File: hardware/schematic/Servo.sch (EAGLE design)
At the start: 23 parts

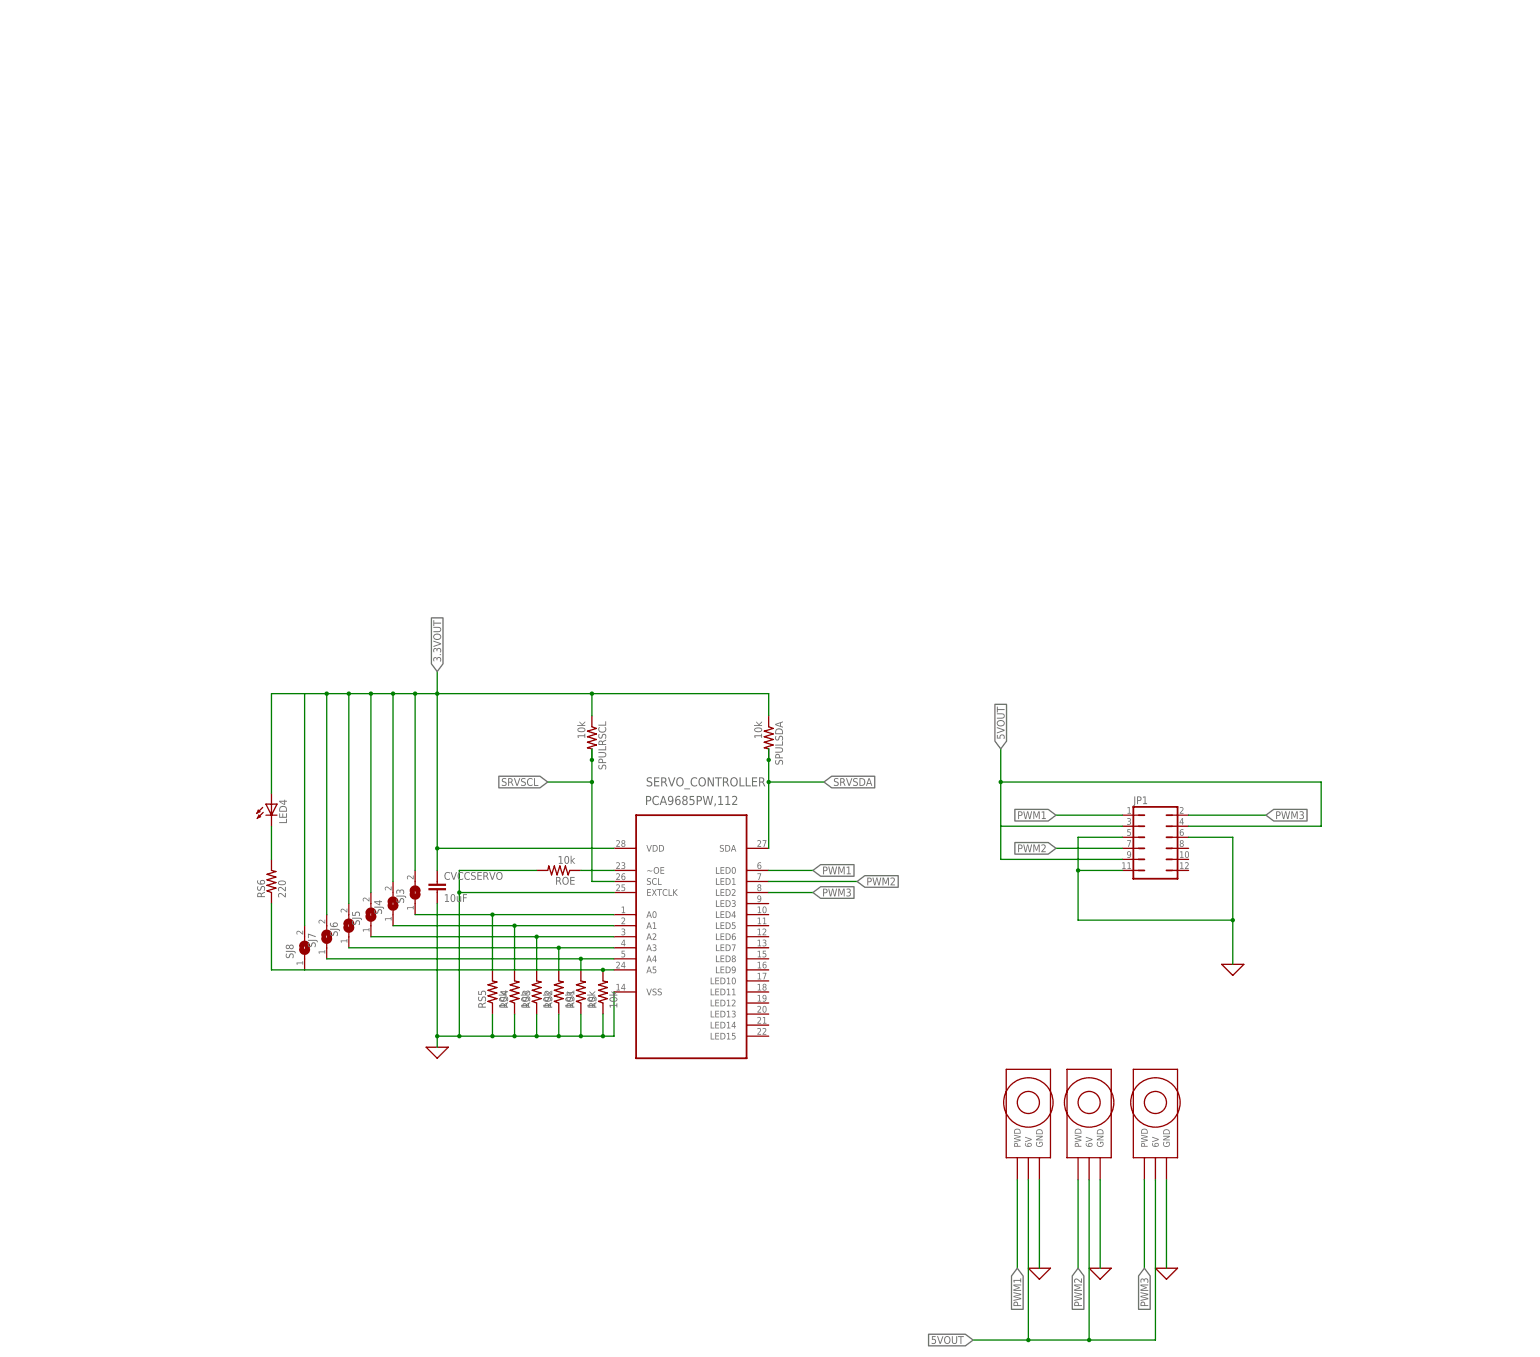
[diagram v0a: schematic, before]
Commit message: Schematic Updates
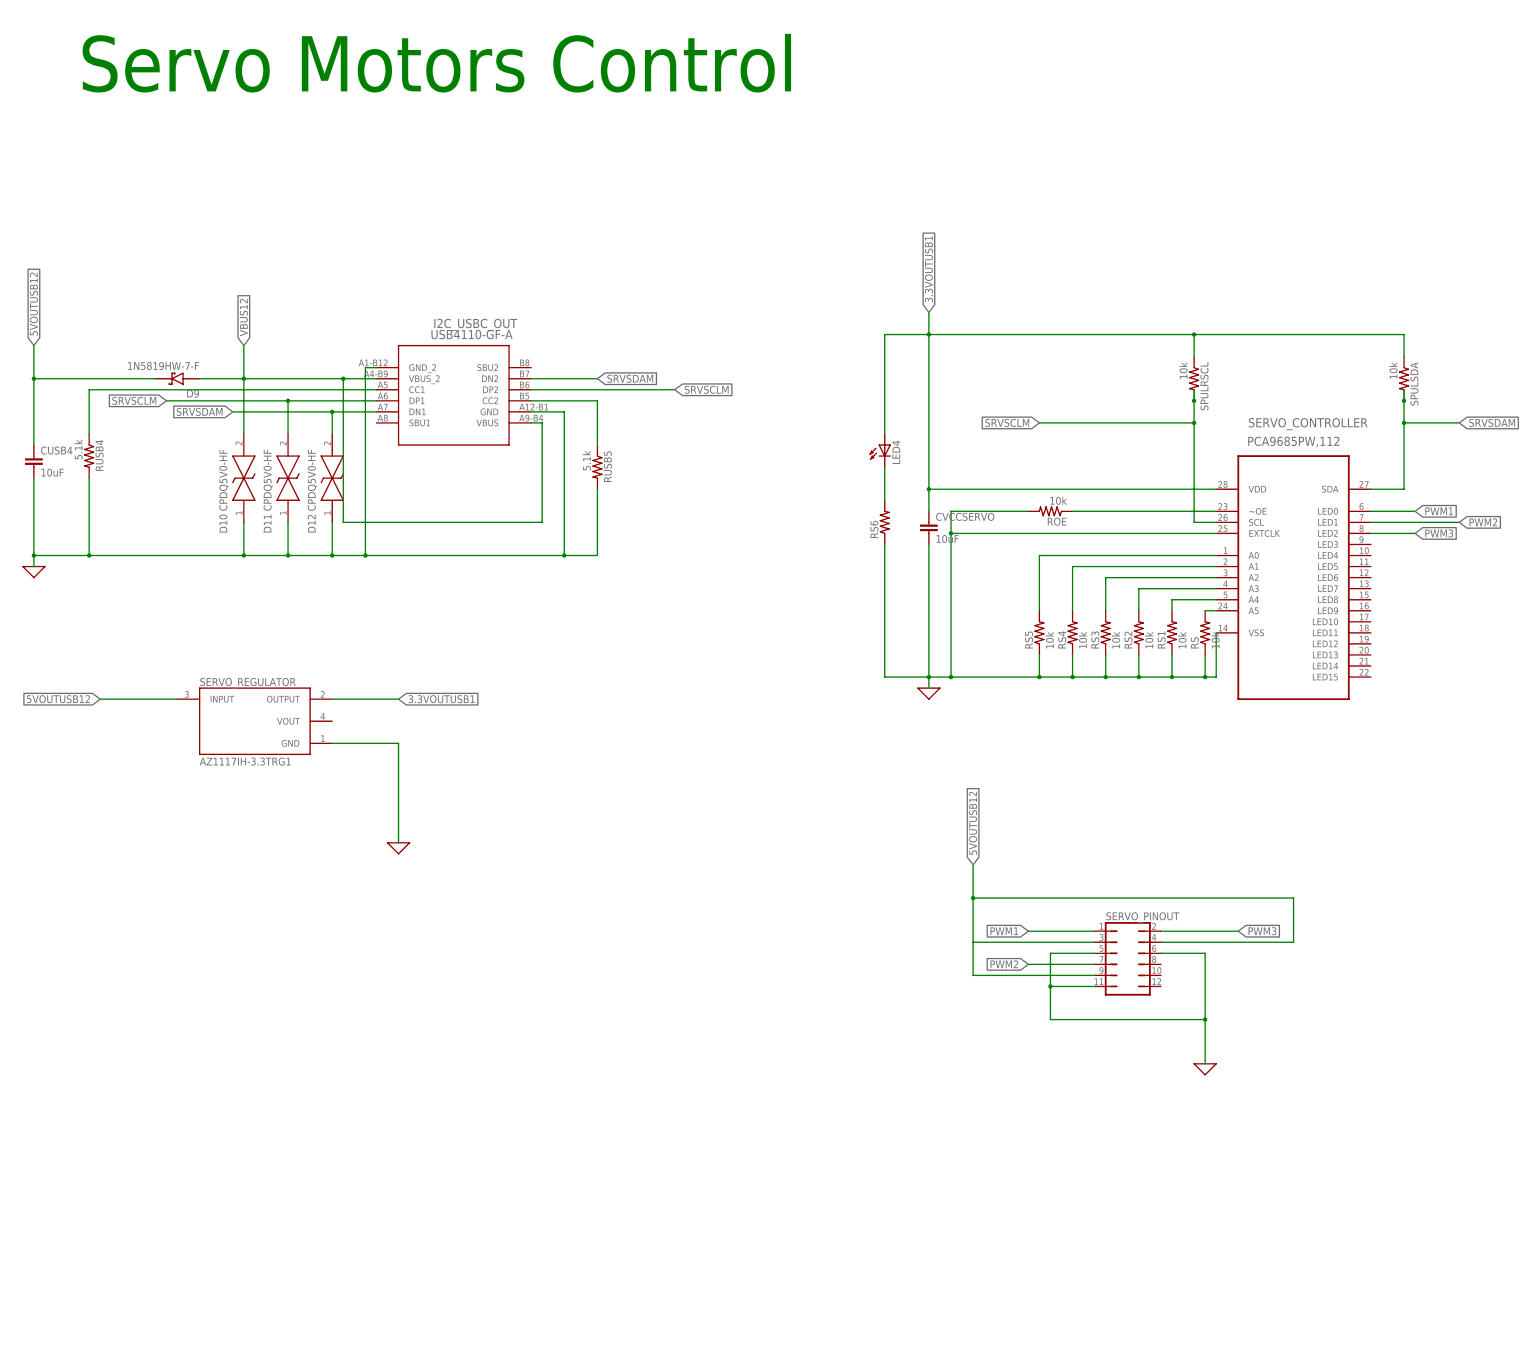
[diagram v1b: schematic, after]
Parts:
- removed JP1: (no value), jumper:JP6Q
- removed SJ3, SJ4, SJ5, SJ6, SJ7, SJ8: (no value), jumper:SJ
- removed U$1, U$2, U$3: SERVO, Motors:SERVO
- added CUSB4: 10uF, rcl:C-EUC0805
- added D10, D11, D12: CPDQ5V0-HF, CPDQ5V0-HF:CPDQ5V0-HF
- added D9: 1N5819HW-7-F, 1N5819HW-7-F:1N5819HW-7-F
- added I2C_USBC_OUT: USB4110-GF-A, USB4110-GF-A:USB4110-GF-A
- added RUSB4, RUSB5: 5.1k, rcl:R-US_M0805
- added SERVO_PINOUT: (no value), jumper:JP6Q
- added SERVO_REGULATOR: AZ1117IH-3.3TRG1, AZ1117IH-3.3TRG1:AZ1117IH-3.3TRG1
- RS6: value 220 -> 2.2k
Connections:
- removed net 0: CVCCSERVO.2, JP1.11, JP1.5, JP1.6, ROE.2, RS.1, RS1.1, RS2.1, RS3.1, RS4.1, RS5.1, SERVO_CONTROLLER.EXTCLK, SERVO_CONTROLLER.VSS, U$1.GND, U$2.GND, U$3.GND
- removed net 3.3VOUT: CVCCSERVO.1, LED4.A, SERVO_CONTROLLER.VDD, SJ3.2, SJ4.2, SJ5.2, SJ6.2, SJ7.2, SJ8.2, SPULRSCL.1, SPULSDA.1
- removed net 5VOUT: JP1.3, JP1.4, JP1.9, U$1.6V, U$2.6V, U$3.6V
- removed net SRVSCL: SERVO_CONTROLLER.SCL, SPULRSCL.2
- removed net SRVSDA: SERVO_CONTROLLER.SDA, SPULSDA.2
- new net 3.3VOUTUSB1: CVCCSERVO.1, LED4.A, SERVO_CONTROLLER.VDD, SERVO_REGULATOR.OUTPUT, SPULRSCL.1, SPULSDA.1
- new net 5VOUTUSB12: CUSB4.1, D9.K, SERVO_PINOUT.3, SERVO_PINOUT.4, SERVO_PINOUT.9, SERVO_REGULATOR.INPUT
- new net GND: CUSB4.2, CVCCSERVO.2, D10.K, D11.K, D12.K, I2C_USBC_OUT.GND, I2C_USBC_OUT.GND_2, ROE.2, RS.1, RS1.1, RS2.1, RS3.1, RS4.1, RS5.1, RS6.1, RUSB4.2, RUSB5.2, SERVO_CONTROLLER.EXTCLK, SERVO_CONTROLLER.VSS, SERVO_PINOUT.11, SERVO_PINOUT.5, SERVO_PINOUT.6, SERVO_REGULATOR.GND
- new net N$64: I2C_USBC_OUT.CC1, RUSB4.1
- new net N$65: I2C_USBC_OUT.CC2, RUSB5.1
- new net SRVSCLM: D11.A, I2C_USBC_OUT.DP1, I2C_USBC_OUT.DP2, SERVO_CONTROLLER.SCL, SPULRSCL.2
- new net SRVSDAM: D12.A, I2C_USBC_OUT.DN1, I2C_USBC_OUT.DN2, SERVO_CONTROLLER.SDA, SPULSDA.2
- new net VBUS12: D10.A, D9.A, I2C_USBC_OUT.VBUS, I2C_USBC_OUT.VBUS_2
- net N$44: no longer SJ4.1
- net N$45: no longer SJ3.1
- net N$46: no longer SJ5.1
- net N$47: no longer SJ6.1
- net N$48: no longer SJ7.1
- net N$49: no longer RS6.1, SJ8.1
- net PWM1: now also SERVO_PINOUT.1; no longer JP1.1, U$1.PWD
- net PWM2: now also SERVO_PINOUT.7; no longer JP1.7, U$2.PWD
- net PWM3: now also SERVO_PINOUT.2; no longer JP1.2, U$3.PWD
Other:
- note added: "Servo Motors Control"
- moved on the sheet: CVCCSERVO, LED4, ROE, RS, RS1, RS2, RS3, RS4, RS5, RS6, SERVO_CONTROLLER, SPULRSCL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

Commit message: Update Servo.sch
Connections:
- net N$39 renamed OE
- net N$44 renamed A1
- net N$45 renamed A0
- net N$46 renamed A2
- net N$47 renamed A3
- net N$48 renamed A4
- net N$49 renamed A5
- net N$50 renamed LED_RS6
- net N$64 renamed CC1_RUSB4
- net N$65 renamed CC2
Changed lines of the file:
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@@
 </segment>
 </net>
-<net name="N$39" class="0">
+<net name="OE" class="0">
 <segment>
 <pinref part="SERVO_CONTROLLER" gate="A" pin="~OE"/>
@@
 </segment>
 </net>
-<net name="N$45" class="0">
+<net name="A0" class="0">
 <segment>
 <pinref part="SERVO_CONTROLLER" gate="A" pin="A0"/>
@@
 </segment>
 </net>
-<net name="N$44" class="0">
+<net name="A1" class="0">
 <segment>
 <pinref part="SERVO_CONTROLLER" gate="A" pin="A1"/>
@@
 </segment>
 </net>
-<net name="N$46" class="0">
+<net name="A2" class="0">
 <segment>
 <pinref part="SERVO_CONTROLLER" gate="A" pin="A2"/>
@@
 </segment>
 </net>
-<net name="N$47" class="0">
+<net name="A3" class="0">
 <segment>
 <pinref part="SERVO_CONTROLLER" gate="A" pin="A3"/>
@@
 </segment>
 </net>
-<net name="N$48" class="0">
+<net name="A4" class="0">
 <segment>
 <pinref part="SERVO_CONTROLLER" gate="A" pin="A4"/>
@@
 </segment>
 </net>
-<net name="N$49" class="0">
+<net name="A5" class="0">
 <segment>
 <pinref part="SERVO_CONTROLLER" gate="A" pin="A5"/>
@@
 </segment>
 </net>
-<net name="N$50" class="0">
+<net name="LED_RS6" class="0">
 <segment>
 <pinref part="LED4" gate="G$1" pin="C"/>
@@
 <pinref part="SPULRSCL" gate="G$1" pin="2"/>
 <wire x1="83.82" y1="111.76" x2="83.82" y2="116.84" width="0.1524" layer="91"/>
-<wire x1="83.82" y1="116.84" x2="83.82" y2="119.38" width="0.1524" layer="91"/>
-<junction x="83.82" y="116.84"/>
 <wire x1="83.82" y1="111.76" x2="48.26" y2="111.76" width="0.1524" layer="91"/>
 <junction x="83.82" y="111.76"/>
@@
 </segment>
 </net>
-<net name="N$64" class="0">
+<net name="CC1_RUSB4" class="0">
 <segment>
 <pinref part="I2C_USBC_OUT" gate="A" pin="CC1"/>
@@
 </segment>
 </net>
-<net name="N$65" class="0">
+<net name="CC2" class="0">
 <segment>
 <pinref part="I2C_USBC_OUT" gate="A" pin="CC2"/>

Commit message: Schematics updates
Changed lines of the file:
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@@
 <parts>
 <part name="SERVO_CONTROLLER" library="PCA9685PW_112" deviceset="PCA9685PW,112" device=""/>
-<part name="X_8" library="ngspice-simulation" library_urn="urn:adsk.eagle:library:527439" deviceset="GND" device=""/>
 <part name="CVCCSERVO" library="rcl" library_urn="urn:adsk.eagle:library:334" deviceset="C-EU" device="C0805" package3d_urn="urn:adsk.eagle:package:23617/2" value="10uF"/>
-<part name="X_9" library="ngspice-simulation" library_urn="urn:adsk.eagle:library:527439" deviceset="GND" device=""/>
 <part name="ROE" library="rcl" library_urn="urn:adsk.eagle:library:334" deviceset="R-US_" device="M0805" package3d_urn="urn:adsk.eagle:package:23556/2" value="10k"/>
 <part name="SPULRSCL" library="rcl" library_urn="urn:adsk.eagle:library:334" deviceset="R-US_" device="M0805" package3d_urn="urn:adsk.eagle:package:23556/2" value="10k"/>
@@
 <part name="D9" library="1N5819HW-7-F" deviceset="1N5819HW-7-F" device=""/>
 <part name="CUSB4" library="rcl" library_urn="urn:adsk.eagle:library:334" deviceset="C-EU" device="C0805" package3d_urn="urn:adsk.eagle:package:23617/2" value="10uF"/>
-<part name="X_16" library="ngspice-simulation" library_urn="urn:adsk.eagle:library:527439" deviceset="GND" device=""/>
 <part name="RUSB4" library="rcl" library_urn="urn:adsk.eagle:library:334" deviceset="R-US_" device="M0805" package3d_urn="urn:adsk.eagle:package:23556/2" value="5.1k"/>
 <part name="RUSB5" library="rcl" library_urn="urn:adsk.eagle:library:334" deviceset="R-US_" device="M0805" package3d_urn="urn:adsk.eagle:package:23556/2" value="5.1k"/>
@@
 <part name="D12" library="CPDQ5V0-HF" deviceset="CPDQ5V0-HF" device=""/>
 <part name="SERVO_REGULATOR" library="AZ1117IH-3.3TRG1" deviceset="AZ1117IH-3.3TRG1" device=""/>
-<part name="X_21" library="ngspice-simulation" library_urn="urn:adsk.eagle:library:527439" deviceset="GND" device=""/>
+<part name="SUPPLY1" library="supply2" library_urn="urn:adsk.eagle:library:372" deviceset="GND" device=""/>
+<part name="SUPPLY2" library="supply2" library_urn="urn:adsk.eagle:library:372" deviceset="GND" device=""/>
+<part name="SUPPLY3" library="supply2" library_urn="urn:adsk.eagle:library:372" deviceset="GND" device=""/>
+<part name="SUPPLY4" library="supply2" library_urn="urn:adsk.eagle:library:372" deviceset="GND" device=""/>
 </parts>
 <sheets>
@@
 <attribute name="VALUE" x="96.01018125" y="106.4809" size="2.08405" layer="96" ratio="10" rot="SR0"/>
 </instance>
-<instance part="X_8" gate="G$1" x="86.36" y="-35.56" smashed="yes"/>
 <instance part="CVCCSERVO" gate="G$1" x="22.86" y="88.9" smashed="yes">
 <attribute name="NAME" x="24.384" y="89.281" size="1.778" layer="95"/>
 <attribute name="VALUE" x="24.384" y="84.201" size="1.778" layer="96"/>
 </instance>
-<instance part="X_9" gate="G$1" x="22.86" y="50.8" smashed="yes"/>
 <instance part="ROE" gate="G$1" x="50.8" y="91.44" smashed="yes" rot="R180">
 <attribute name="NAME" x="54.61" y="89.9414" size="1.778" layer="95" rot="R180"/>
@@
 <attribute name="VALUE" x="-181.356" y="99.441" size="1.778" layer="96"/>
 </instance>
-<instance part="X_16" gate="G$1" x="-182.88" y="78.74" smashed="yes"/>
 <instance part="RUSB4" gate="G$1" x="-170.18" y="104.14" smashed="yes" rot="R270">
 <attribute name="NAME" x="-168.6814" y="107.95" size="1.778" layer="95" rot="R270"/>
@@
 <attribute name="VALUE" x="-144.78" y="33.02" size="1.778" layer="96"/>
 </instance>
-<instance part="X_21" gate="G$1" x="-99.06" y="15.24" smashed="yes"/>
+<instance part="SUPPLY1" gate="GND" x="86.36" y="-38.1" smashed="yes">
+<attribute name="VALUE" x="84.455" y="-41.275" size="1.778" layer="96"/>
+</instance>
+<instance part="SUPPLY2" gate="GND" x="22.86" y="48.26" smashed="yes">
+<attribute name="VALUE" x="20.955" y="45.085" size="1.778" layer="96"/>
+</instance>
+<instance part="SUPPLY3" gate="GND" x="-182.88" y="76.2" smashed="yes">
+<attribute name="VALUE" x="-184.785" y="73.025" size="1.778" layer="96"/>
+</instance>
+<instance part="SUPPLY4" gate="GND" x="-99.06" y="12.7" smashed="yes">
+<attribute name="VALUE" x="-100.965" y="9.525" size="1.778" layer="96"/>
+</instance>
 </instances>
 <busses>
@@
 <pinref part="SERVO_PINOUT" gate="B" pin="4"/>
 <pinref part="SERVO_PINOUT" gate="B" pin="9"/>
+<junction x="33.02" y="-7.62"/>
 </segment>
 <segment>
@@
 <wire x1="50.8" y1="-10.16" x2="50.8" y2="-17.78" width="0.1524" layer="91"/>
 <junction x="50.8" y="-17.78"/>
-<pinref part="X_8" gate="G$1" pin="0"/>
 <pinref part="SERVO_PINOUT" gate="B" pin="5"/>
 <pinref part="SERVO_PINOUT" gate="B" pin="6"/>
 <pinref part="SERVO_PINOUT" gate="B" pin="11"/>
+<pinref part="SUPPLY1" gate="GND" pin="GND"/>
 </segment>
 <segment>
@@
 <wire x1="22.86" y1="53.34" x2="22.86" y2="50.8" width="0.1524" layer="91"/>
 <junction x="22.86" y="53.34"/>
-<pinref part="X_9" gate="G$1" pin="0"/>
 <pinref part="SERVO_CONTROLLER" gate="A" pin="EXTCLK"/>
 <wire x1="88.9" y1="86.36" x2="27.94" y2="86.36" width="0.1524" layer="91"/>
@@
 <wire x1="12.7" y1="83.82" x2="12.7" y2="53.34" width="0.1524" layer="91"/>
 <wire x1="12.7" y1="53.34" x2="22.86" y2="53.34" width="0.1524" layer="91"/>
+<pinref part="SUPPLY2" gate="GND" pin="GND"/>
 </segment>
 <segment>
 <pinref part="CUSB4" gate="G$1" pin="2"/>
 <wire x1="-182.88" y1="99.06" x2="-182.88" y2="81.28" width="0.1524" layer="91"/>
-<pinref part="X_16" gate="G$1" pin="0"/>
 <pinref part="RUSB4" gate="G$1" pin="2"/>
 <wire x1="-182.88" y1="81.28" x2="-182.88" y2="78.74" width="0.1524" layer="91"/>
@@
 <wire x1="-114.3" y1="88.9" x2="-114.3" y2="81.28" width="0.1524" layer="91"/>
 <junction x="-114.3" y="81.28"/>
+<pinref part="SUPPLY3" gate="GND" pin="GND"/>
 </segment>
 <segment>
@@
 <wire x1="-114.3" y1="38.1" x2="-99.06" y2="38.1" width="0.1524" layer="91"/>
 <wire x1="-99.06" y1="38.1" x2="-99.06" y2="15.24" width="0.1524" layer="91"/>
-<pinref part="X_21" gate="G$1" pin="0"/>
+<pinref part="SUPPLY4" gate="GND" pin="GND"/>
 </segment>
 </net>
@@
 </sheet>
 </sheets>
+<errors>
+</errors>
 </schematic>
 </drawing>

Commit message: Servo Updated
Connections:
- net 3.3VOUTUSB1: now also SERVO_REGULATOR.VOUT
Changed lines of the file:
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@@
 <pinref part="SERVO_REGULATOR" gate="G$1" pin="OUTPUT"/>
 <label x="-99.06" y="48.26" size="1.778" layer="95" xref="yes"/>
-<wire x1="-114.3" y1="48.26" x2="-99.06" y2="48.26" width="0.1524" layer="91"/>
+<wire x1="-114.3" y1="48.26" x2="-104.14" y2="48.26" width="0.1524" layer="91"/>
+<pinref part="SERVO_REGULATOR" gate="G$1" pin="VOUT"/>
+<wire x1="-104.14" y1="48.26" x2="-99.06" y2="48.26" width="0.1524" layer="91"/>
+<wire x1="-114.3" y1="43.18" x2="-104.14" y2="43.18" width="0.1524" layer="91"/>
+<wire x1="-104.14" y1="43.18" x2="-104.14" y2="48.26" width="0.1524" layer="91"/>
+<junction x="-104.14" y="48.26"/>
 </segment>
 </net>
